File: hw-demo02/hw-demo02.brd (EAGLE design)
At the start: 63.2 x 63.5 mm, 14 parts

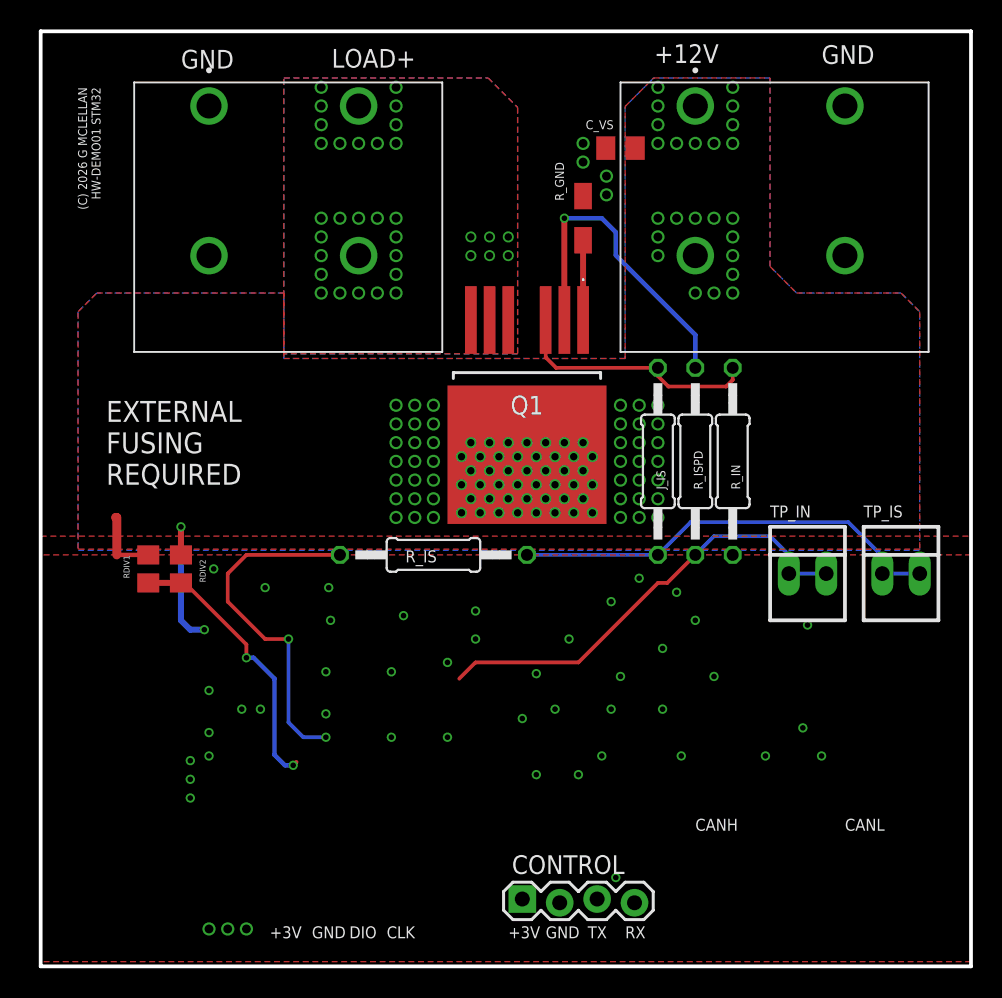
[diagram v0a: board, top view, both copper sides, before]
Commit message: removed unused traces and vias, layout tweaks
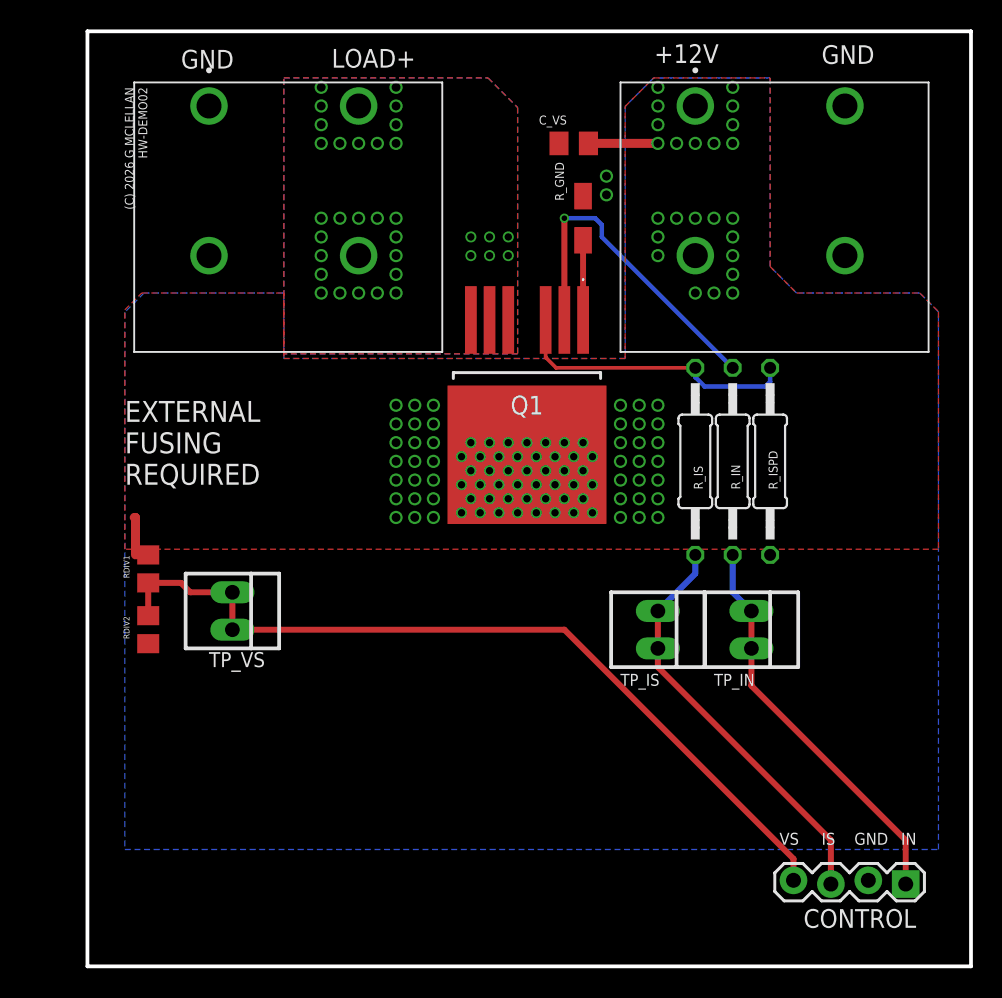
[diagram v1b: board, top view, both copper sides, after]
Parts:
- removed J_IS: 0R0, rcl:0207/12
- added TP_VS: (no value), con-molex:22-23-2021
- moved CONTROL 26.1 mm to (60.0, 5.71), turned to 180 degrees
- moved R_IS 18.9 mm to (45.7, 34.3), turned to 270 degrees
- moved TP_IS 16.9 mm to (43.2, 22.9), turned to 270 degrees
- moved TP_IN 5.39 mm to (49.5, 22.9), turned to 270 degrees
- moved RDIV2 4.69 mm to (8.57, 22.9), turned to 90 degrees
- moved C_VS 3.19 mm to (37.5, 55.9)
- moved R_IN 2.54 mm to (48.3, 34.3)
- moved R_ISPD 2.54 mm to (50.8, 34.3)
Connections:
- removed net N$2: J_IS.2, R_IS.1, TP_IS.1, TP_IS.2
- net IS: now also R_IS.1; no longer J_IS.1
- net IS_OUT: now also TP_IS.1, TP_IS.2
- net VS_OUT: now also TP_VS.1, TP_VS.2
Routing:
- net VS_OUT: track 18.8 -> 56.8 mm, vias 2 -> 0
- net N$2: track 29.7 -> 0.00 mm
- net GND: track 10.1 -> 0.00 mm, vias 52 -> 2
- net IS_OUT: track 23.9 -> 28.3 mm, vias 2 -> 0
- net IN: track 30.7 -> 27.2 mm
- net +12V: track 4.77 -> 8.21 mm
- net IS: track 17.4 -> 20.1 mm
- net CTL3`: track 22.2 -> 23.0 mm
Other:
- board size 63.2 x 63.5 mm -> 60 x 63.5 mm
- board text added: "(C) 2026 G MCLELLAN HW-DEMO02"
- board text added: "IN"
- board text added: "IS"
- board text added: "VS"
- board text removed: "(C) 2026 G MCLELLAN HW-DEMO01 STM32"
- board text removed: "+3V"
- board text removed: "CANH"
- board text removed: "CANL"
- board text removed: "CLK"
- board text removed: "DIO"
- board text removed: "RX"
- board text removed: "TX"

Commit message: layout tweaks and layer stitching, added ground test point
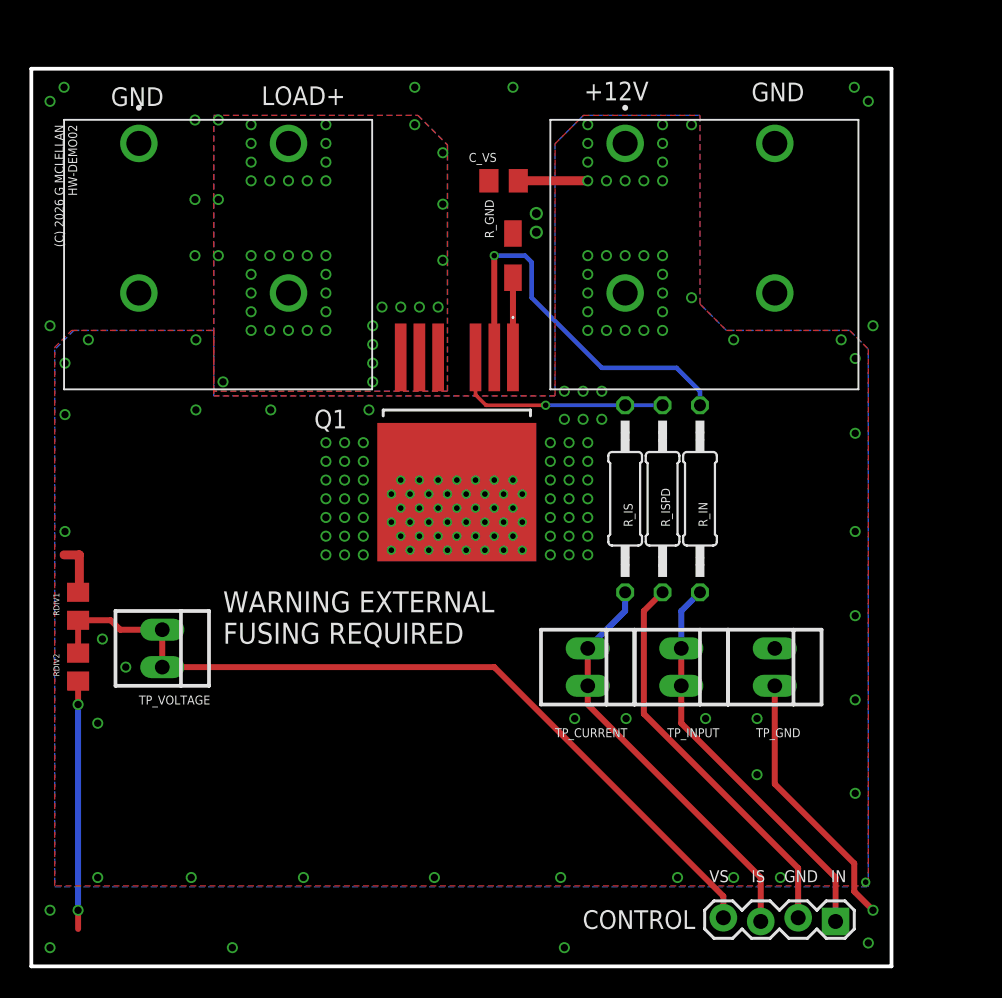
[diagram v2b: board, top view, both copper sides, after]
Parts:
- removed TP_IN, TP_IS, TP_VS: (no value), con-molex:22-23-2021
- added TP_CURRENT, TP_GND, TP_INPUT, TP_VOLTAGE: (no value), con-molex:22-23-2021
- moved R_ISPD 7.73 mm to (43.5, 31.8)
- moved LOAD+ 5.40 mm to (13.0, 50.8)
- moved Q1 5.40 mm to (29.5, 34.9)
- moved CONTROL 5.40 mm to (55.2, 3.17)
- moved C_VS 5.40 mm to (32.7, 53.3)
- moved R_GND 5.40 mm to (33.3, 48.3)
- moved +12V 5.40 mm to (46.0, 50.8)
- moved RDIV1 5.40 mm to (3.81, 24.4)
- moved RDIV2 5.40 mm to (3.81, 20.3)
- moved R_IS 5.40 mm to (41.0, 31.8)
- moved R_IN 3.38 mm to (46.0, 31.8)
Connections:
- net GND: now also TP_GND.1, TP_GND.2
- net IN: now also TP_INPUT.1, TP_INPUT.2; no longer TP_IN.1, TP_IN.2
- net IS_OUT: now also TP_CURRENT.1, TP_CURRENT.2; no longer TP_IS.1, TP_IS.2
- net VS_OUT: now also TP_VOLTAGE.1, TP_VOLTAGE.2; no longer TP_VS.1, TP_VS.2
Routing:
- net GND: track 0.00 -> 61.8 mm, vias 2 -> 21
- net IS: track 20.1 -> 15.5 mm, vias 0 -> 1
- net CTL3`: track 23.0 -> 27.1 mm
- net +12V: track 8.21 -> 8.31 mm, vias 111 -> 155
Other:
- board size 60 x 63.5 mm -> 58.4 x 61 mm
- board text added: "WARNING EXTERNAL FUSING REQUIRED"
- board text removed: "EXTERNAL FUSING REQUIRED"
